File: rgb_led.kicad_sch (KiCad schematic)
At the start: 52 parts

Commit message: More refinement
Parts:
- gave numbers to parts that had none: 46
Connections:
- net 5V renamed +5V
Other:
- company: (none) -> Student Robotics
- title: (none) -> Raspberry Pi HAT

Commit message: Schematic revision S1
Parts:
- D17, D18, D19, D20: value (none) -> FM-B2020RGBA-HG
- Q11, Q12, Q13, Q14, Q15, Q16: value (none) -> 2N7002KDW
- R47, R49, R51, R56, R58, R60, R65, R67, R69, R74, R76, R78: value (none) -> 10k
- R48, R50, R53, R57, R59, R62, R66, R68, R71, R75, R77, R80: value (none) -> 1k
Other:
- moved on the sheet: D19, Q14A, Q14B, Q15A, R65, R66, R67, R68, R69, R70, R71, R72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

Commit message: Pre-review improvements
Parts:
- Q11, Q12, Q13, Q14, Q15, Q16: footprint (none) -> Package_TO_SOT_SMD:SOT-363_SC-70-6
- R47, R48, R49, R50, R51, R53, R56, R57, R58, R59, R60, R62, R65, R66, R67, R68, R69, R71, R74, R75, R76, R77, R78, R80: footprint (none) -> Resistor_SMD:R_0402_1005Metric
- R52, R61, R70, R79: value (none) -> 330R; footprint (none) -> Resistor_SMD:R_0402_1005Metric
- R54, R55, R63, R64, R72, R73, R81, R82: value (none) -> 220R; footprint (none) -> Resistor_SMD:R_0402_1005Metric

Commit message: Add remaining footprints
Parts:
- D17, D18, D19, D20: footprint (none) -> project_footprints:FM-B2020RGBA-HG
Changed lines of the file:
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@@
     (property "Reference" "D19" (id 0) (at 193.04 79.502 0))
     (property "Value" "FM-B2020RGBA-HG" (id 1) (at 196.85 97.79 0))
-    (property "Footprint" "" (id 2) (at 193.04 90.17 0)
+    (property "Footprint" "project_footprints:FM-B2020RGBA-HG" (id 2) (at 193.04 90.17 0)
       (effects (font (size 1.27 1.27)) hide)
     )
@@
     (property "Reference" "D20" (id 0) (at 257.81 22.352 0))
     (property "Value" "FM-B2020RGBA-HG" (id 1) (at 262.255 40.64 0))
-    (property "Footprint" "" (id 2) (at 257.81 33.02 0)
+    (property "Footprint" "project_footprints:FM-B2020RGBA-HG" (id 2) (at 257.81 33.02 0)
       (effects (font (size 1.27 1.27)) hide)
     )
@@
     (property "Reference" "D18" (id 0) (at 124.46 22.352 0))
     (property "Value" "FM-B2020RGBA-HG" (id 1) (at 128.905 40.64 0))
-    (property "Footprint" "" (id 2) (at 124.46 33.02 0)
+    (property "Footprint" "project_footprints:FM-B2020RGBA-HG" (id 2) (at 124.46 33.02 0)
       (effects (font (size 1.27 1.27)) hide)
     )
@@
     (property "Reference" "D17" (id 0) (at 73.66 117.602 0))
     (property "Value" "FM-B2020RGBA-HG" (id 1) (at 78.105 135.89 0))
-    (property "Footprint" "" (id 2) (at 73.66 128.27 0)
-      (effects (font (size 1.27 1.27)) hide)
-    )
+    (property "Footprint" "project_footprints:FM-B2020RGBA-HG" (id 2) (at 73.66 128.27 0)
+      (effects (font (size 1.27 1.27)) hide)
+    )

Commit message: Updates for version S2
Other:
- title: Raspberry Pi HAT -> KCH - Raspberry Pi HAT
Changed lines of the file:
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@@
   (paper "A4")
   (title_block
-    (title "Raspberry Pi HAT")
-    (date "2022-05-14")
-    (rev "S1.1")
+    (title "KCH - Raspberry Pi HAT")
+    (date "2022-05-17")
+    (rev "S2")
     (company "Student Robotics")
     (comment 1 "RGB LEDs")

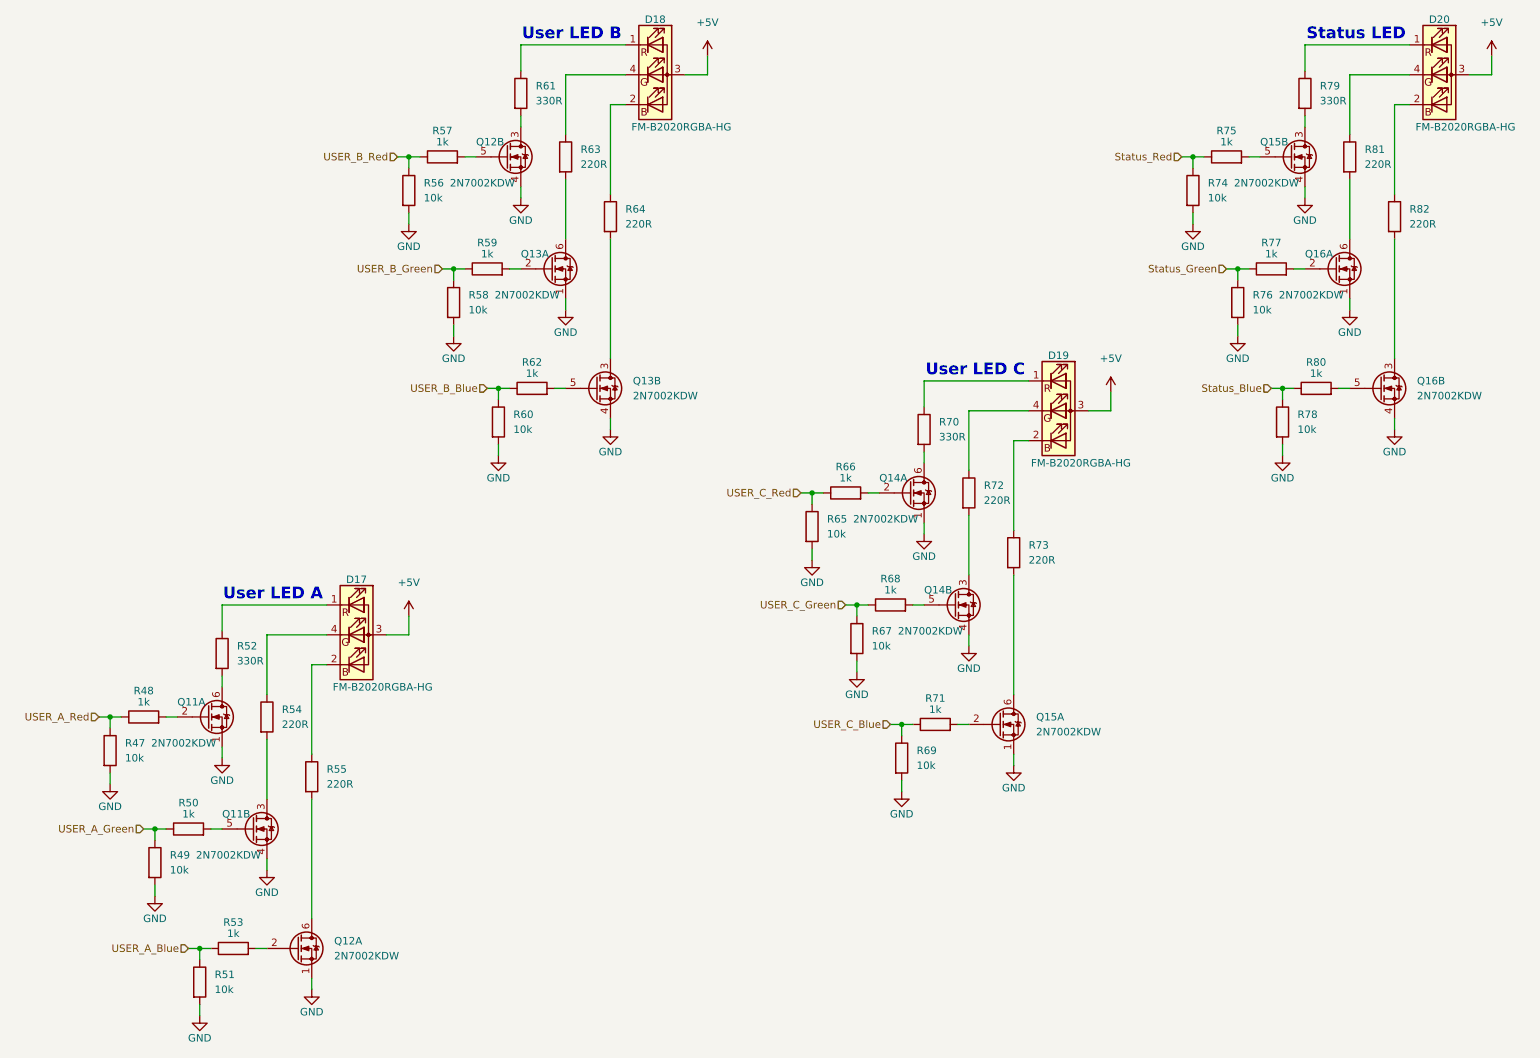
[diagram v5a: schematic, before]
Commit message: V1 of the layout
In line with spec.md and subject to review.
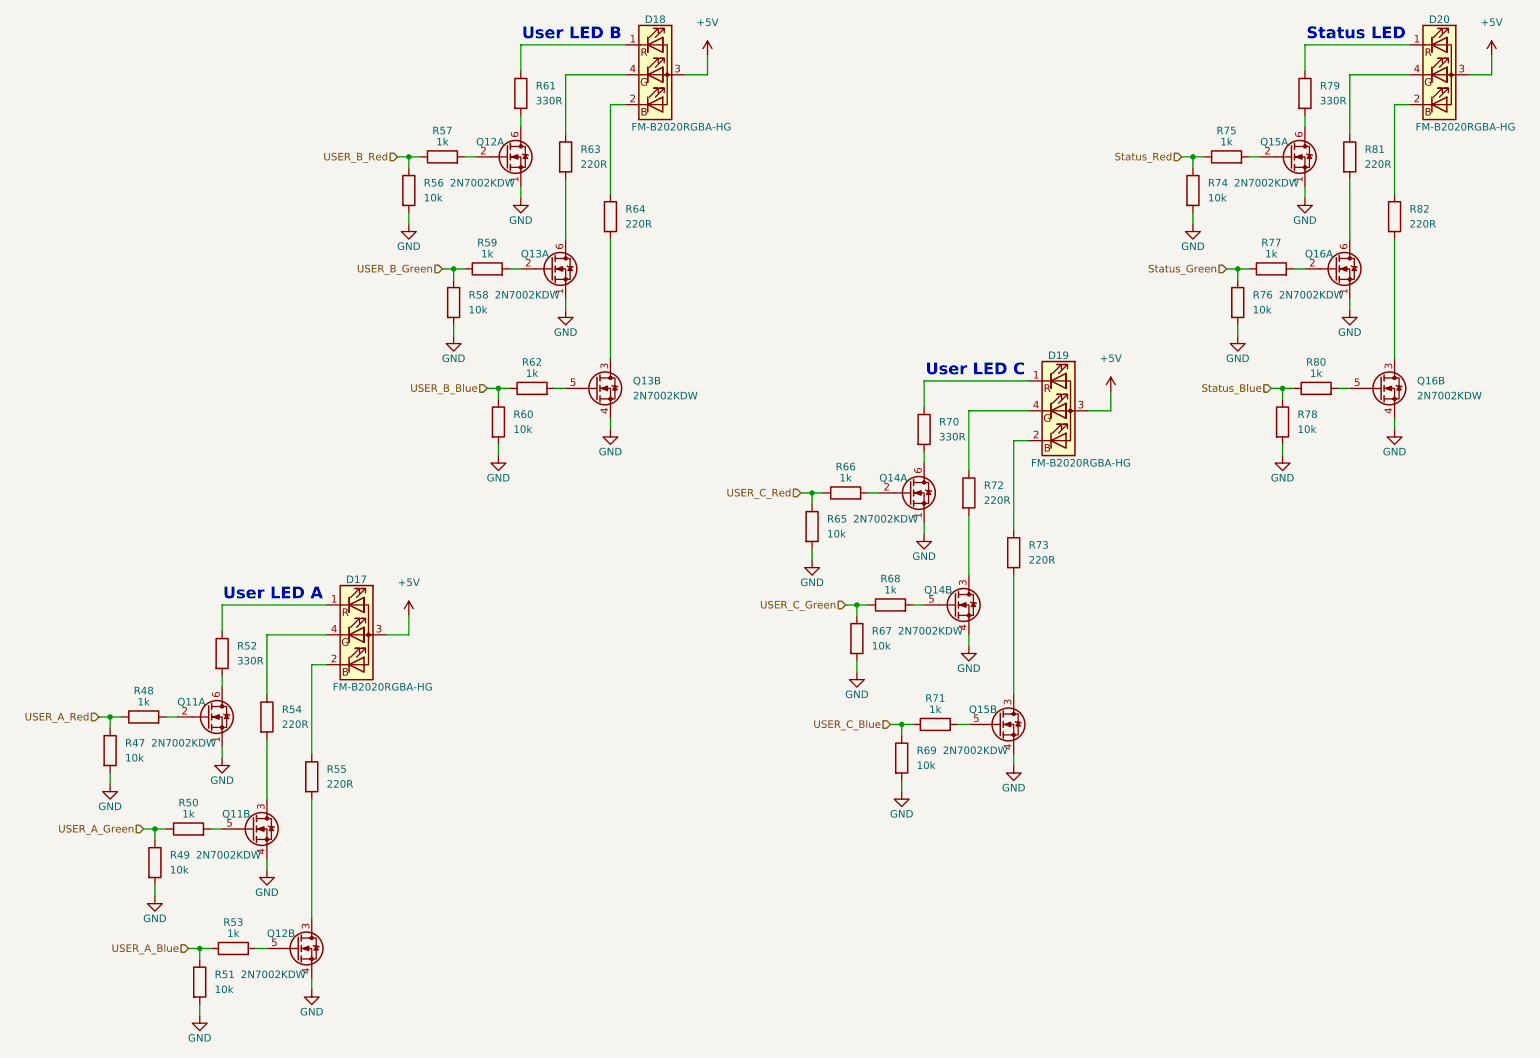
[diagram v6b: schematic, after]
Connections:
- net at R79.2: now also Q15.6 (D); no longer Q15.3 (D)
- net at R61.2: now also Q12.6 (D); no longer Q12.3 (D)
- net at R53.2: now also Q12.5 (G); no longer Q12.2 (G)
- net at R55.2: now also Q12.3 (D); no longer Q12.6 (D)
- net at R75.2: now also Q15.2 (G); no longer Q15.5 (G)
- net at R73.2: now also Q15.3 (D); no longer Q15.6 (D)
- net at R57.2: now also Q12.2 (G); no longer Q12.5 (G)
- net at R71.2: now also Q15.5 (G); no longer Q15.2 (G)
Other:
- moved on the sheet: Q12A, Q12B, Q15A, Q15B
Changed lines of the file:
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@@
     (pin "2")
   )
-  (symbol (lib_id "Device:Q_Dual_NMOS_S1G1D2S2G2D1") (at 63.5 180.34 0) (unit 1)
-    (in_bom yes) (on_board yes) (fields_autoplaced)
-    (property "Reference" "Q12" (id 0) (at 69.85 179.0699 0)
-      (effects (font (size 1.27 1.27)) (justify left))
-    )
-    (property "Value" "2N7002KDW" (id 1) (at 69.85 181.6099 0)
-      (effects (font (size 1.27 1.27)) (justify left))
-    )
-    (property "Footprint" "Package_TO_SOT_SMD:SOT-363_SC-70-6" (id 2) (at 68.58 180.34 0)
-      (effects (font (size 1.27 1.27)) hide)
-    )
-    (property "Datasheet" "https://datasheet.lcsc.com/lcsc/1808151859_PANJIT-International-2N7002KDW_C106992.pdf" (id 3) (at 68.58 180.34 0)
+  (symbol (lib_id "Device:Q_Dual_NMOS_S1G1D2S2G2D1") (at 99.06 45.72 0) (unit 1)
+    (in_bom yes) (on_board yes)
+    (property "Reference" "Q12" (id 0) (at 93.98 43.18 0)
+      (effects (font (size 1.27 1.27)) (justify left))
+    )
+    (property "Value" "2N7002KDW" (id 1) (at 89.535 50.165 0)
+      (effects (font (size 1.27 1.27)) (justify left))
+    )
+    (property "Footprint" "Package_TO_SOT_SMD:SOT-363_SC-70-6" (id 2) (at 104.14 45.72 0)
+      (effects (font (size 1.27 1.27)) hide)
+    )
+    (property "Datasheet" "https://datasheet.lcsc.com/lcsc/1808151859_PANJIT-International-2N7002KDW_C106992.pdf" (id 3) (at 104.14 45.72 0)
       (effects (font (size 1.27 1.27)) hide)
     )
@@
     (pin "1")
   )
-  (symbol (lib_id "Device:Q_Dual_NMOS_S1G1D2S2G2D1") (at 99.06 45.72 0) (unit 2)
-    (in_bom yes) (on_board yes)
-    (property "Reference" "Q12" (id 0) (at 93.98 43.18 0)
-      (effects (font (size 1.27 1.27)) (justify left))
-    )
-    (property "Value" "2N7002KDW" (id 1) (at 89.535 50.165 0)
-      (effects (font (size 1.27 1.27)) (justify left))
-    )
-    (property "Footprint" "Package_TO_SOT_SMD:SOT-363_SC-70-6" (id 2) (at 104.14 45.72 0)
-      (effects (font (size 1.27 1.27)) hide)
-    )
-    (property "Datasheet" "https://datasheet.lcsc.com/lcsc/1808151859_PANJIT-International-2N7002KDW_C106992.pdf" (id 3) (at 104.14 45.72 0)
+  (symbol (lib_id "Device:Q_Dual_NMOS_S1G1D2S2G2D1") (at 63.5 180.34 0) (unit 2)
+    (in_bom yes) (on_board yes)
+    (property "Reference" "Q12" (id 0) (at 58.42 177.8 0)
+      (effects (font (size 1.27 1.27)) (justify left))
+    )
+    (property "Value" "2N7002KDW" (id 1) (at 53.975 184.785 0)
+      (effects (font (size 1.27 1.27)) (justify left))
+    )
+    (property "Footprint" "Package_TO_SOT_SMD:SOT-363_SC-70-6" (id 2) (at 68.58 180.34 0)
+      (effects (font (size 1.27 1.27)) hide)
+    )
+    (property "Datasheet" "https://datasheet.lcsc.com/lcsc/1808151859_PANJIT-International-2N7002KDW_C106992.pdf" (id 3) (at 68.58 180.34 0)
       (effects (font (size 1.27 1.27)) hide)
     )
@@
     (pin "1")
   )
-  (symbol (lib_id "Device:Q_Dual_NMOS_S1G1D2S2G2D1") (at 232.41 45.72 0) (unit 2)
-    (in_bom yes) (on_board yes)
-    (property "Reference" "Q15" (id 0) (at 227.33 43.18 0)
-      (effects (font (size 1.27 1.27)) (justify left))
-    )
-    (property "Value" "2N7002KDW" (id 1) (at 222.885 50.165 0)
-      (effects (font (size 1.27 1.27)) (justify left))
-    )
-    (property "Footprint" "Package_TO_SOT_SMD:SOT-363_SC-70-6" (id 2) (at 237.49 45.72 0)
-      (effects (font (size 1.27 1.27)) hide)
-    )
-    (property "Datasheet" "https://datasheet.lcsc.com/lcsc/1808151859_PANJIT-International-2N7002KDW_C106992.pdf" (id 3) (at 237.49 45.72 0)
+  (symbol (lib_id "Device:Q_Dual_NMOS_S1G1D2S2G2D1") (at 182.88 142.24 0) (unit 2)
+    (in_bom yes) (on_board yes)
+    (property "Reference" "Q15" (id 0) (at 177.8 139.7 0)
+      (effects (font (size 1.27 1.27)) (justify left))
+    )
+    (property "Value" "2N7002KDW" (id 1) (at 173.355 146.685 0)
+      (effects (font (size 1.27 1.27)) (justify left))
+    )
+    (property "Footprint" "Package_TO_SOT_SMD:SOT-363_SC-70-6" (id 2) (at 187.96 142.24 0)
+      (effects (font (size 1.27 1.27)) hide)
+    )
+    (property "Datasheet" "https://datasheet.lcsc.com/lcsc/1808151859_PANJIT-International-2N7002KDW_C106992.pdf" (id 3) (at 187.96 142.24 0)
       (effects (font (size 1.27 1.27)) hide)
     )
@@
     (pin "2")
   )
-  (symbol (lib_id "Device:Q_Dual_NMOS_S1G1D2S2G2D1") (at 182.88 142.24 0) (unit 1)
-    (in_bom yes) (on_board yes) (fields_autoplaced)
-    (property "Reference" "Q15" (id 0) (at 189.23 140.9699 0)
-      (effects (font (size 1.27 1.27)) (justify left))
-    )
-    (property "Value" "2N7002KDW" (id 1) (at 189.23 143.5099 0)
-      (effects (font (size 1.27 1.27)) (justify left))
-    )
-    (property "Footprint" "Package_TO_SOT_SMD:SOT-363_SC-70-6" (id 2) (at 187.96 142.24 0)
-      (effects (font (size 1.27 1.27)) hide)
-    )
-    (property "Datasheet" "https://datasheet.lcsc.com/lcsc/1808151859_PANJIT-International-2N7002KDW_C106992.pdf" (id 3) (at 187.96 142.24 0)
-      (effects (font (size 1.27 1.27)) hide)
-    )
+  (symbol (lib_id "Device:Q_Dual_NMOS_S1G1D2S2G2D1") (at 232.41 45.72 0) (unit 1)
+    (in_bom yes) (on_board yes)
+    (property "Reference" "Q15" (id 0) (at 227.33 43.18 0)
+      (effects (font (size 1.27 1.27)) (justify left))
+    )
+    (property "Value" "2N7002KDW" (id 1) (at 222.885 50.165 0)
+      (effects (font (size 1.27 1.27)) (justify left))
+    )
+    (property "Footprint" "Package_TO_SOT_SMD:SOT-363_SC-70-6" (id 2) (at 237.49 45.72 0)
+      (effects (font (size 1.27 1.27)) hide)
+    )
+    (property "Datasheet" "https://datasheet.lcsc.com/lcsc/1808151859_PANJIT-International-2N7002KDW_C106992.pdf" (id 3) (at 237.49 45.72 0)
+      (effects (font (size 1.27 1.27)) hide)
+    )
